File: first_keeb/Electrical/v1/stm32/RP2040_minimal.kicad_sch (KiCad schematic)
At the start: 65 parts, among them J1 Conn_01x04_Socket, P1 USB-TYPE-C-016, Q1 BSS138, SW1 TS-1187A-B-A-B, SW2 TS-1187A-B-A-B, SW3 BUTT1, SW4 BUTT3, SW5 BUTT2, U1 ME6208A44M3G, U2 ME6212C25M5G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

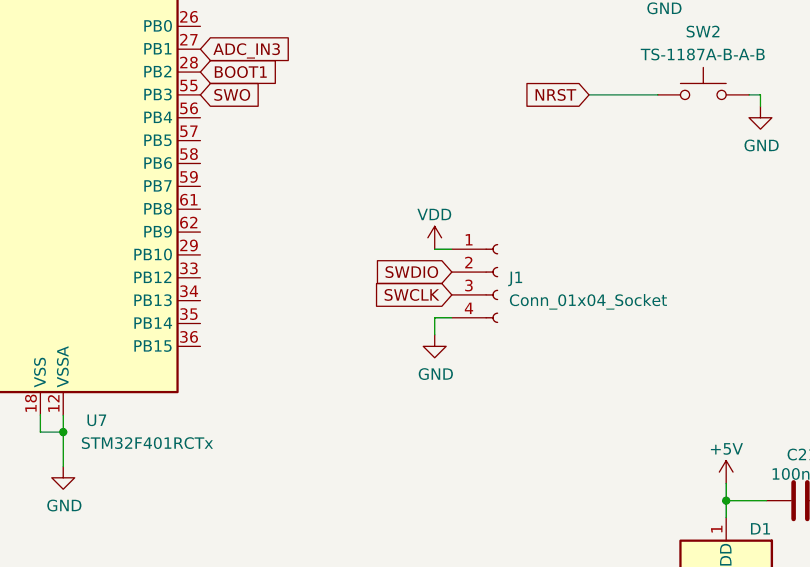
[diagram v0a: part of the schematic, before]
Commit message: switches swdio and swclk on stm to match rp2040
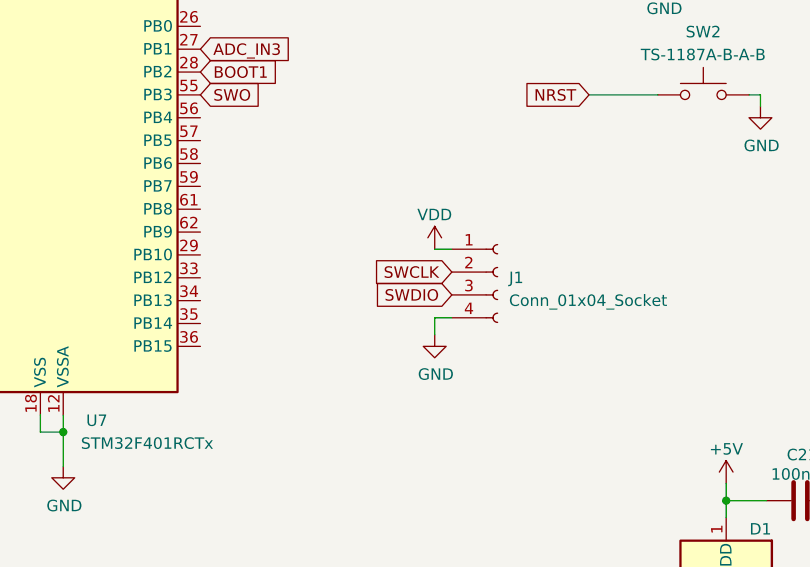
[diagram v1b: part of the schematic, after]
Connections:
- net SWCLK: now also J1.2 (Pin_2); no longer J1.3 (Pin_3)
- net SWDIO: now also J1.3 (Pin_3); no longer J1.2 (Pin_2)
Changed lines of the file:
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@@
+    )
+  )
+  (global_label "SWCLK" (shape input) (at 135.89 149.225 180)
+    (effects (font (size 1.27 1.27)) (justify right))
+    (property "Intersheetrefs" "${INTERSHEET_REFS}" (at 135.89 149.225 0)
+      (effects (font (size 1.27 1.27)) hide)
     )
   )
@@
     (effects (font (size 1.27 1.27)) (justify right))
     (property "Intersheetrefs" "${INTERSHEET_REFS}" (at 147.32 97.155 0)
+      (effects (font (size 1.27 1.27)) hide)
+    )
+  )
+  (global_label "SWDIO" (shape input) (at 135.89 151.765 180)
+    (effects (font (size 1.27 1.27)) (justify right))
+    (property "Intersheetrefs" "${INTERSHEET_REFS}" (at 135.89 151.765 0)
       (effects (font (size 1.27 1.27)) hide)
     )
@@
     )
   )
-  (global_label "SWDIO" (shape input) (at 135.89 149.225 180)
-    (effects (font (size 1.27 1.27)) (justify right))
-    (property "Intersheetrefs" "${INTERSHEET_REFS}" (at 135.89 149.225 0)
-      (effects (font (size 1.27 1.27)) hide)
-    )
-  )
   (global_label "OSC_IN" (shape input) (at 74.93 93.98 180)
     (effects (font (size 1.27 1.27)) (justify right))
@@
     )
   )
-  (global_label "SWCLK" (shape input) (at 135.89 151.765 180)
-    (effects (font (size 1.27 1.27)) (justify right))
-    (property "Intersheetrefs" "${INTERSHEET_REFS}" (at 135.89 151.765 0)
-      (effects (font (size 1.27 1.27)) hide)
-    )
-  )

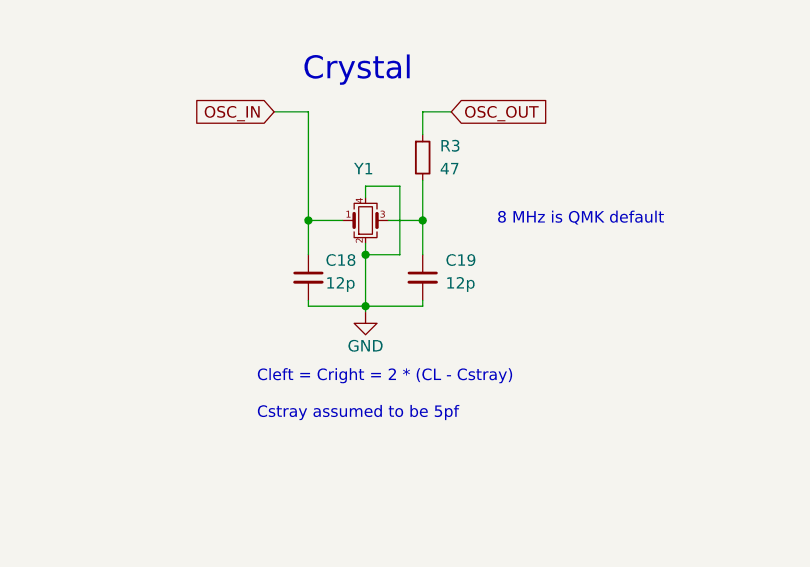
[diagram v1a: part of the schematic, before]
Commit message: moves plates together
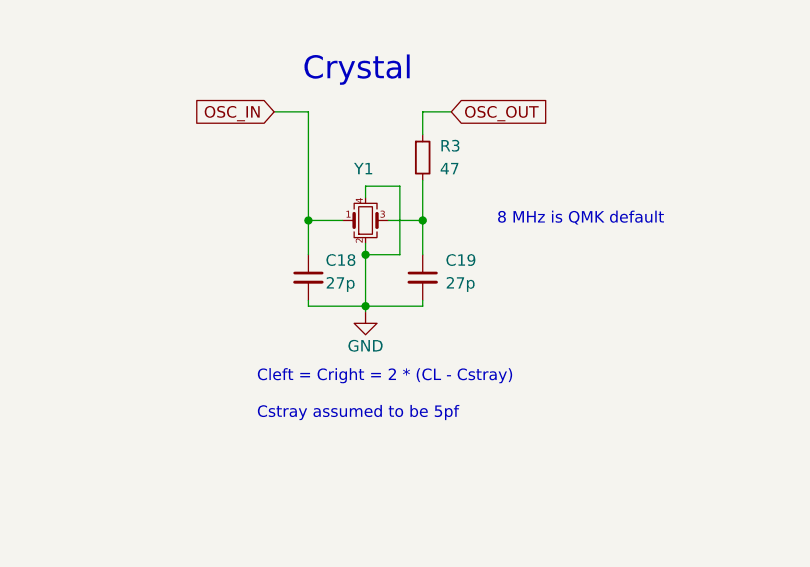
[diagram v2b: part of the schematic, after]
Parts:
- C18, C19: value 12p -> 27p; LCSC Part # C1547 -> (none)
- Y1: value 8MHz -> 12MHz; LCSC Part # C13738 -> C9002
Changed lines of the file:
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@@
       (effects (font (size 1.27 1.27)) (justify left))
     )
-    (property "Value" "8MHz" (at 219.075 97.155 0)
+    (property "Value" "12MHz" (at 219.075 97.155 0)
       (effects (font (size 1.27 1.27)) (justify left) hide)
     )
@@
       (effects (font (size 1.27 1.27)) hide)
     )
-    (property "Datasheet" "~" (at 222.25 102.87 0)
+    (property "Datasheet" "X322512MSB4SI" (at 222.25 102.87 0)
       (effects (font (size 1.27 1.27)) hide)
     )
-    (property "LCSC Part #" "C13738" (at 222.25 102.87 0)
+    (property "LCSC Part #" "C9002" (at 222.25 102.87 0)
       (effects (font (size 1.27 1.27)) hide)
     )
@@
       (effects (font (size 1.27 1.27)) (justify left))
     )
-    (property "Value" "12p" (at 217.805 109.855 0)
+    (property "Value" "27p" (at 217.805 109.855 0)
       (effects (font (size 1.27 1.27)) (justify left))
     )
@@
       (effects (font (size 1.27 1.27)) hide)
     )
-    (property "LCSC Part #" "C1547" (at 215.9 109.22 0)
+    (property "LCSC Part #" "" (at 215.9 109.22 0)
       (effects (font (size 1.27 1.27)) hide)
     )
@@
       (effects (font (size 1.27 1.27)) (justify left))
     )
-    (property "Value" "12p" (at 231.14 109.855 0)
+    (property "Value" "27p" (at 231.14 109.855 0)
       (effects (font (size 1.27 1.27)) (justify left))
     )
@@
       (effects (font (size 1.27 1.27)) hide)
     )
-    (property "LCSC Part #" "C1547" (at 228.6 109.22 0)
+    (property "LCSC Part #" "" (at 228.6 109.22 0)
       (effects (font (size 1.27 1.27)) hide)
     )

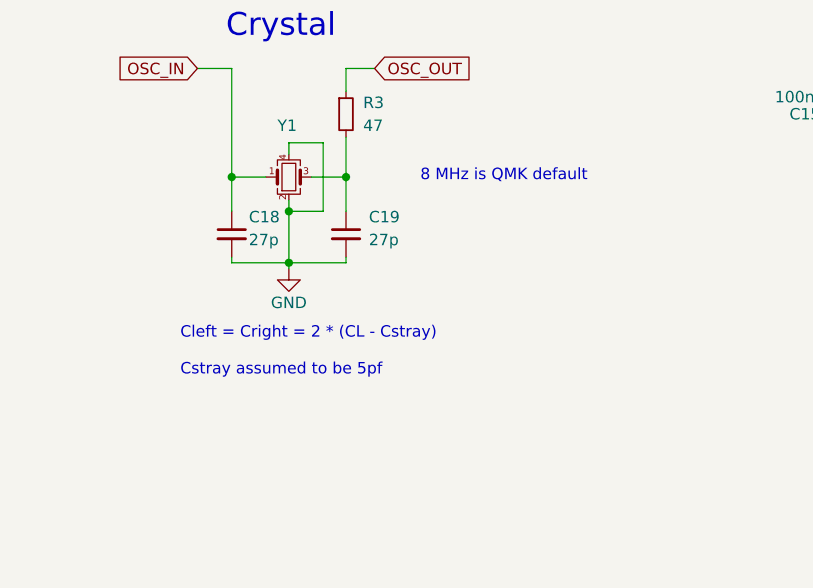
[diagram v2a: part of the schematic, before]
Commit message: changes caps to match 12MHz crystal
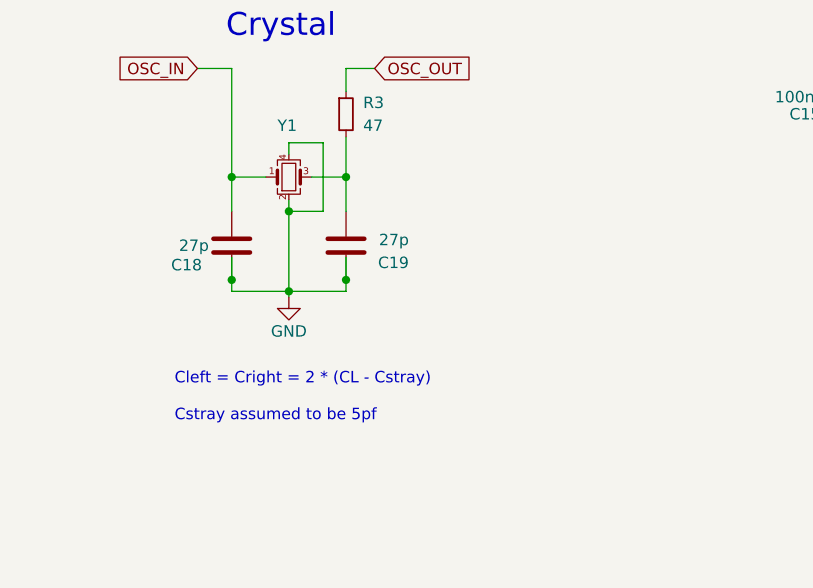
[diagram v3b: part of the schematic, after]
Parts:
- removed C18, C19: 27p, Capacitor_SMD:C_0402_1005Metric, symbol Device:C_Small
- added C18, C19: 27p, Capacitor_SMD:C_0402_1005Metric, symbol Device:C
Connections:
- net GND: now also C18.1, C19.1
- net OSC_IN: now also C18.2
- net at R3.2, Y1.3: now also C19.2
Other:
- note removed: "8 MHz is QMK default"
